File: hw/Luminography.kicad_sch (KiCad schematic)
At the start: 143 parts, among them J1 USB_C_Receptacle_PowerOnly_6P, J2 Conn_01x04, Q1 2N7002, SW1 SW_Push, SW2 SW_Push, U1 LTC4054ES5-4.2, U10 MMC5603NJ, U100 BH1750FVI-TR, U101 BH1750FVI-TR, U102 BH1750FVI-TR, U103 BH1750FVI-TR, U104 BH1750FVI-TR, U105 BH1750FVI-TR, U106 BH1750FVI-TR, U107 BH1750FVI-TR, U108 BH1750FVI-TR, U109 BH1750FVI-TR, U11 BMI270, U110 BH1750FVI-TR, U111 BH1750FVI-TR, U112 BH1750FVI-TR, U113 BH1750FVI-TR, U114 BH1750FVI-TR, U115 BH1750FVI-TR, U116 BH1750FVI-TR, U117 BH1750FVI-TR, U118 BH1750FVI-TR, U119 BH1750FVI-TR, U12 MAX98357AETE+, U120 BH1750FVI-TR, U121 BH1750FVI-TR, U122 BH1750FVI-TR, U123 BH1750FVI-TR, U2 XS3A1T3157GMX, U200 HD107S, U201 HD107S, U202 HD107S, U203 HD107S, U204 HD107S, U205 HD107S, U206 HD107S, U207 HD107S, U208 HD107S, U209 HD107S, U210 HD107S, U211 HD107S, U212 HD107S, U213 HD107S, U214 HD107S, U215 HD107S, U216 HD107S, U217 HD107S, U218 HD107S, U219 HD107S, U220 HD107S, U221 HD107S, U222 HD107S, U223 HD107S, U3 SPX3819M5-L-3-3, U4 TPS61220DCK, U5 MAX17048G+T10, U6 STM32G030C8Tx, U7 ZJY128R-IG01, U8 TXS0102DCT, U9 W25Q16JVUXIQ, Y1 32MHz 12pF

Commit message: 🚧 Maybe finally close to done
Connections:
- net LED_CLK: now also U6.18 (PA7), U8.4 (A2); no longer U6.16 (PA5), U8.5 (A1)
- net LED_CLK_5V: now also U8.1 (B2); no longer U8.8 (B1)
- net LED_DATA: now also U6.16 (PA5), U8.5 (A1); no longer U6.18 (PA7), U8.4 (A2)
- net LED_DATA_5V: now also U8.8 (B1); no longer U8.1 (B2)
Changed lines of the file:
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@@
     )
   )
-  (global_label "LED_CLK" (shape bidirectional) (at 76.2 85.725 0) (fields_autoplaced)
-    (effects (font (size 1.27 1.27)) (justify left))
-    (property "Intersheetrefs" "${INTERSHEET_REFS}" (at 88.2793 85.725 0)
+  (global_label "LED_CLK" (shape bidirectional) (at 76.2 90.805 0) (fields_autoplaced)
+    (effects (font (size 1.27 1.27)) (justify left))
+    (property "Intersheetrefs" "${INTERSHEET_REFS}" (at 88.2793 90.805 0)
       (effects (font (size 1.27 1.27)) (justify left) hide)
     )
@@
     )
   )
-  (global_label "LED_DATA_5V" (shape bidirectional) (at 155.575 123.19 0) (fields_autoplaced)
-    (effects (font (size 1.27 1.27)) (justify left))
-    (property "Intersheetrefs" "${INTERSHEET_REFS}" (at 171.7667 123.19 0)
+  (global_label "LED_DATA_5V" (shape bidirectional) (at 155.575 118.11 0) (fields_autoplaced)
+    (effects (font (size 1.27 1.27)) (justify left))
+    (property "Intersheetrefs" "${INTERSHEET_REFS}" (at 171.7667 118.11 0)
       (effects (font (size 1.27 1.27)) (justify left) hide)
     )
@@
     )
   )
-  (global_label "LED_DATA" (shape bidirectional) (at 76.2 90.805 0) (fields_autoplaced)
-    (effects (font (size 1.27 1.27)) (justify left))
-    (property "Intersheetrefs" "${INTERSHEET_REFS}" (at 89.126 90.805 0)
+  (global_label "LED_DATA" (shape bidirectional) (at 76.2 85.725 0) (fields_autoplaced)
+    (effects (font (size 1.27 1.27)) (justify left))
+    (property "Intersheetrefs" "${INTERSHEET_REFS}" (at 89.126 85.725 0)
       (effects (font (size 1.27 1.27)) (justify left) hide)
     )
@@
     )
   )
-  (global_label "LED_CLK_5V" (shape bidirectional) (at 155.575 118.11 0) (fields_autoplaced)
-    (effects (font (size 1.27 1.27)) (justify left))
-    (property "Intersheetrefs" "${INTERSHEET_REFS}" (at 170.92 118.11 0)
+  (global_label "LED_CLK_5V" (shape bidirectional) (at 155.575 123.19 0) (fields_autoplaced)
+    (effects (font (size 1.27 1.27)) (justify left))
+    (property "Intersheetrefs" "${INTERSHEET_REFS}" (at 170.92 123.19 0)
       (effects (font (size 1.27 1.27)) (justify left) hide)
     )
@@
     )
   )
-  (global_label "LED_DATA" (shape bidirectional) (at 135.255 123.19 180) (fields_autoplaced)
-    (effects (font (size 1.27 1.27)) (justify right))
-    (property "Intersheetrefs" "${INTERSHEET_REFS}" (at 122.329 123.19 0)
+  (global_label "LED_DATA" (shape bidirectional) (at 135.255 118.11 180) (fields_autoplaced)
+    (effects (font (size 1.27 1.27)) (justify right))
+    (property "Intersheetrefs" "${INTERSHEET_REFS}" (at 122.329 118.11 0)
       (effects (font (size 1.27 1.27)) (justify right) hide)
     )
@@
     )
   )
-  (global_label "LED_CLK" (shape bidirectional) (at 135.255 118.11 180) (fields_autoplaced)
-    (effects (font (size 1.27 1.27)) (justify right))
-    (property "Intersheetrefs" "${INTERSHEET_REFS}" (at 123.1757 118.11 0)
-      (effects (font (size 1.27 1.27)) (justify right) hide)
-    )
+  (global_label "LED_CLK" (shape bidirectional) (at 135.255 123.19 180) (fields_autoplaced)
+    (effects (font (size 1.27 1.27)) (justify right))
+    (property "Intersheetrefs" "${INTERSHEET_REFS}" (at 123.1757 123.19 0)
+      (effects (font (size 1.27 1.27)) (justify right) hide)
+    )

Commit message: Updates before submission
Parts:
- renumbered U11 to U10, U10 to U11
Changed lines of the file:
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@@
   (symbol (lib_id "MMC5603NJ:MMC5603NJ") (at 93.98 178.435 0) (unit 1)
     (in_bom yes) (on_board yes) (dnp no) (fields_autoplaced)
-    (property "Reference" "U10" (at 106.68 171.45 0)
+    (property "Reference" "U11" (at 106.68 171.45 0)
       (effects (font (size 1.27 1.27)))
     )
@@
       (project "Luminography"
         (path "/0d1277fd-8d7e-44b8-97b8-165ee2ab6faa"
-          (reference "U10") (unit 1)
+          (reference "U11") (unit 1)
         )
       )
@@
   (symbol (lib_id "BMI270:BMI270") (at 128.905 175.895 0) (unit 1)
     (in_bom yes) (on_board yes) (dnp no)
-    (property "Reference" "U11" (at 151.13 163.83 0)
+    (property "Reference" "U10" (at 151.13 163.83 0)
       (effects (font (size 1.27 1.27)) (justify left))
     )
@@
       (project "Luminography"
         (path "/0d1277fd-8d7e-44b8-97b8-165ee2ab6faa"
-          (reference "U11") (unit 1)
-        )
-      )
+          (reference "U10") (unit 1)
+        )
+      )

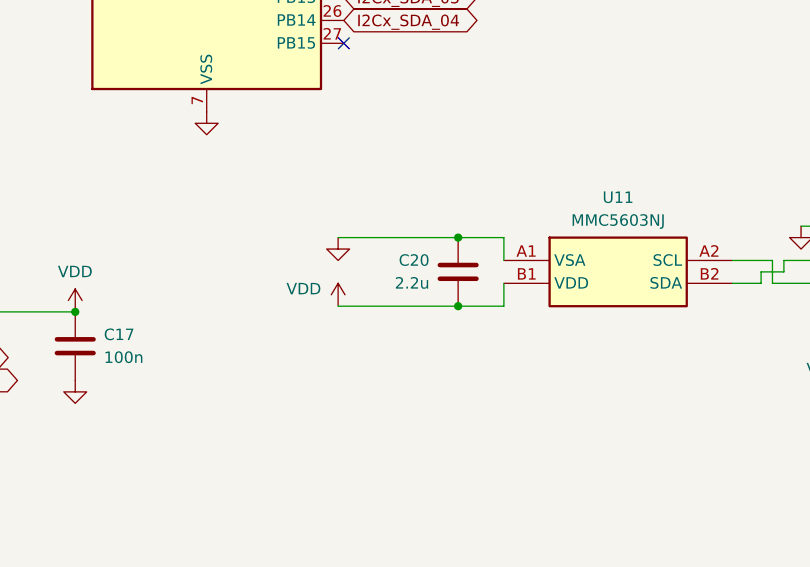
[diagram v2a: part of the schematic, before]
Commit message: Update PCB design file to match actual assembly
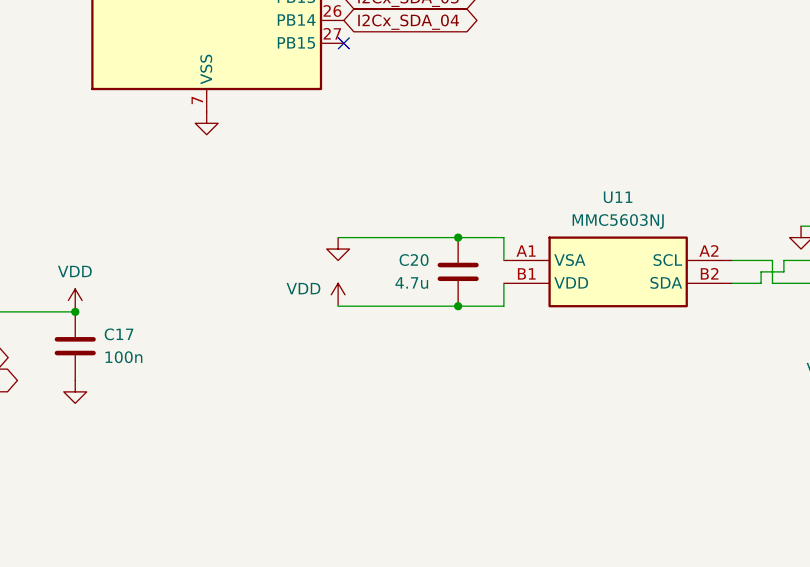
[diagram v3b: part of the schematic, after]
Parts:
- C20: value 2.2u -> 4.7u
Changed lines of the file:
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@@
       (effects (font (size 1.27 1.27)) (justify left))
     )
-    (property "Value" "2.2u" (at 85.725 180.975 0)
+    (property "Value" "4.7u" (at 85.725 180.975 0)
       (effects (font (size 1.27 1.27)) (justify left))
     )

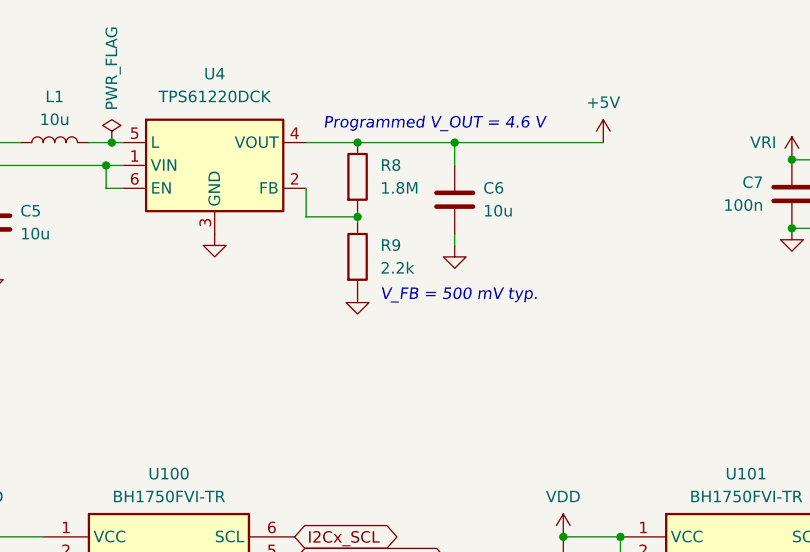
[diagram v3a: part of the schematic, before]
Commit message: Fix incorrect resistor value
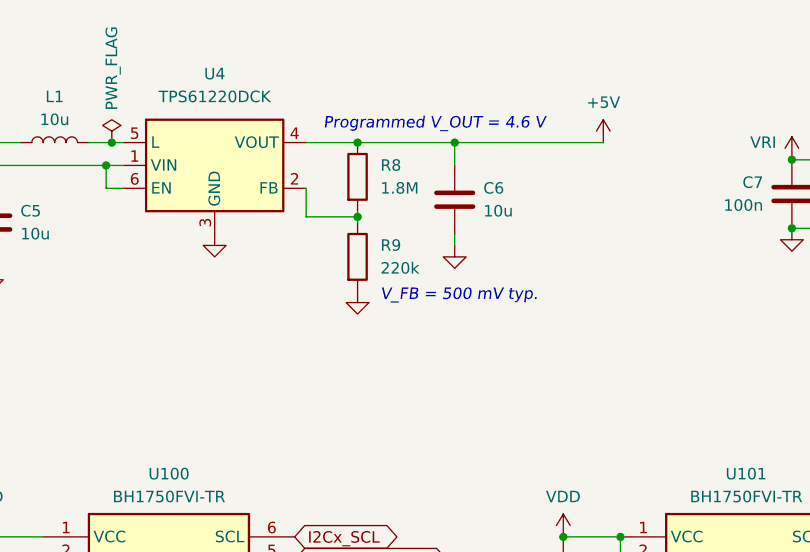
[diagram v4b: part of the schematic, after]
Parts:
- R9: value 2.2k -> 220k
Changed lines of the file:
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@@
       (effects (font (size 1.27 1.27)) (justify left))
     )
-    (property "Value" "2.2k" (at 346.075 39.37 0)
+    (property "Value" "220k" (at 346.075 39.37 0)
       (effects (font (size 1.27 1.27)) (justify left))
     )
